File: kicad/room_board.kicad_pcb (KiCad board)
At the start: 2 copper layers, 40.6 x 58.4 mm, 21 parts, among them K1 CONN_3, U1 MSP430G2452IN20, U2 7805, U3 DHT

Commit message: update files sent to osh park for board creation
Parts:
- added HDR5: AB2_HDR02-1, ab2_header:AB2_HDR_M02-1V, F.Cu at (115.6, 54.6)
- moved SYM 10.2 mm to (114.3, 66.0)
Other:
- board text added: "2014-10-05"
- board text removed: "2014-10-01"
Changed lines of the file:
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@@
-(kicad_pcb (version 4) (host pcbnew "(2014-09-18 BZR 5141)-product")
+(kicad_pcb (version 4) (host pcbnew "(2014-10-04 BZR 5163)-product")
   (general
-    (links 46)
+    (links 48)
     (no_connects 0)
-    (area 102.679499 48.069499 143.700501 106.870501)
+    (area 89.565478 48.069499 155.318334 112.490001)
     (thickness 1.6)
     (drawings 18)
     (tracks 127)
     (zones 0)
-    (modules 21)
+    (modules 22)
     (nets 26)
   )
   (page A4)
   (layers
-    (0 F.Cu signal)
+    (0 F.Cu signal hide)
     (31 B.Cu signal)
     (32 B.Adhes user)
@@
   )
   (setup
-    (last_trace_width 0.8128)
+    (last_trace_width 0.254)
     (user_trace_width 0.254)
     (user_trace_width 0.381)
@@
     (visible_elements FFFFFF7F)
     (pcbplotparams
-      (layerselection 0x03fff_00000000)
-      (usegerberextensions false)
+      (layerselection 0x03fff_80000001)
+      (usegerberextensions true)
       (excludeedgelayer true)
       (linewidth 0.100000)
@@
   )
   (module Symbols:Symbol_OSHW-Logo_SilkScreen (layer B.Cu)
-    (at 114.3 55.88)
+    (at 114.3 66.04)
     (descr "Symbol, OSHW-Logo, Silk Screen,")
     (tags "Symbol, OSHW-Logo, Silk Screen,")
@@
     (fp_line (start 0.35052 -0.89916) (end 0.7493 -1.89992) (layer B.SilkS) (width 0.381))
   )
+  (module ab2_header:AB2_HDR_M02-1V (layer F.Cu)
+    (at 115.57 54.61 90)
+    (fp_text reference HDR5 (at 0 2.54 90) (layer F.SilkS)
+      (effects (font (size 0.8128 0.8128) (thickness 0.0762)))
+    )
+    (fp_text value AB2_HDR02-1 (at 0 -2.54 90) (layer F.SilkS)
+      (effects (font (size 0.8128 0.8128) (thickness 0.0762)))
+    )
+    (fp_line (start -1.905 -1.27) (end -0.635 -1.27) (layer F.SilkS) (width 0.127))
+    (fp_line (start -0.635 -1.27) (end 0 -0.635) (layer F.SilkS) (width 0.127))
+    (fp_line (start 0 -0.635) (end 0.635 -1.27) (layer F.SilkS) (width 0.127))
+    (fp_line (start 0.635 -1.27) (end 1.905 -1.27) (layer F.SilkS) (width 0.127))
+    (fp_line (start 1.905 -1.27) (end 2.54 -0.635) (layer F.SilkS) (width 0.127))
+    (fp_line (start 2.54 -0.635) (end 2.54 0.635) (layer F.SilkS) (width 0.127))
+    (fp_line (start 2.54 0.635) (end 1.905 1.27) (layer F.SilkS) (width 0.127))
+    (fp_line (start 1.905 1.27) (end 0.635 1.27) (layer F.SilkS) (width 0.127))
+    (fp_line (start 0.635 1.27) (end 0 0.635) (layer F.SilkS) (width 0.127))
+    (fp_line (start 0 0.635) (end -0.635 1.27) (layer F.SilkS) (width 0.127))
+    (fp_line (start -0.635 1.27) (end -1.905 1.27) (layer F.SilkS) (width 0.127))
+    (fp_line (start -1.905 1.27) (end -2.54 0.635) (layer F.SilkS) (width 0.127))
+    (fp_line (start -2.54 0.635) (end -2.54 -0.635) (layer F.SilkS) (width 0.127))
+    (fp_line (start -2.54 -0.635) (end -1.905 -1.27) (layer F.SilkS) (width 0.127))
+    (pad 1 thru_hole rect (at -1.27 0 90) (size 1.6764 1.6764) (drill 1.016) (layers *.Cu *.Mask F.SilkS)
+      (net 1 +5V))
+    (pad 2 thru_hole circle (at 1.27 0 90) (size 1.6764 1.6764) (drill 1.016) (layers *.Cu *.Mask F.SilkS)
+      (net 2 GND))
+    (model ab2_header/AB2_HDR_M01-1V.wrl
+      (at (xyz -0.05 0 0))
+      (scale (xyz 0.3937 0.3937 0.3937))
+      (rotate (xyz 0 0 0))
+    )
+    (model ab2_header/AB2_HDR_M01-1V.wrl
+      (at (xyz 0.05 0 0))
+      (scale (xyz 0.3937 0.3937 0.3937))
+      (rotate (xyz 0 0 0))
+    )
+  )
   (gr_text PROGRAM (at 138.43 81.28 90) (layer F.SilkS)
     (effects (font (size 1 1) (thickness 0.25)))
@@
     (effects (font (size 1 1) (thickness 0.25)))
   )
-  (gr_text 2014-10-01 (at 104.14 54.61 90) (layer F.SilkS)
+  (gr_text 2014-10-05 (at 104.14 54.61 90) (layer F.SilkS)
     (effects (font (size 1 1) (thickness 0.25)))
   )
-  (gr_text PIR (at 111.76 54.61 90) (layer F.SilkS)
+  (gr_text PIR (at 109.22 63.5 90) (layer F.SilkS)
     (effects (font (size 1 1) (thickness 0.25)))
   )

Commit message: update kicad schematic
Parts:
- HDR2: value AB2_HDR04-2 -> NRF24L01
- HDR4: value AB2_HDR03-1 -> PROGRAM
- HDR5: value AB2_HDR02-1 -> POWER
- U1: value MSP430G2452IN20 -> MSP430G2553IN20
- moved U1 0.13 mm to (120.8, 88.9)

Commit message: move dht to border
The former position of the DHT was under the nrf24l01.
Fixes #4.
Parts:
- added HDR6: EN_POWER_LED, ab2_header:AB2_HDR_M02-1V, F.Cu at (114.6, 64.8)
- moved U3 8.53 mm to (137.7, 91.4)
- moved SYM 7.47 mm to (106.9, 67.3)
- moved D1 2.41 mm to (139.6, 102.9)
- moved R4 1.65 mm to (121.5, 67.3)
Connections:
- R4 pad 1: +3.3V -> Net-(HDR6-Pad2)
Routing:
- net GND: track 147.7 -> 125.2 mm
- net /DHT_DATA: track 10.2 -> 17.6 mm
- net Net-(HDR6-Pad2): track 0.00 -> 3.70 mm
- net /MOSI: track 25.0 -> 28.4 mm
- net Net-(D1-Pad1): track 5.08 -> 7.49 mm
- net /MISO: track 26.2 -> 28.6 mm
- net Net-(D3-Pad1): track 4.34 -> 5.99 mm
- net +3.3V: track 97.1 -> 98.1 mm
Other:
- board text added: "room board v0.2"
- board text removed: "room board v0.1"

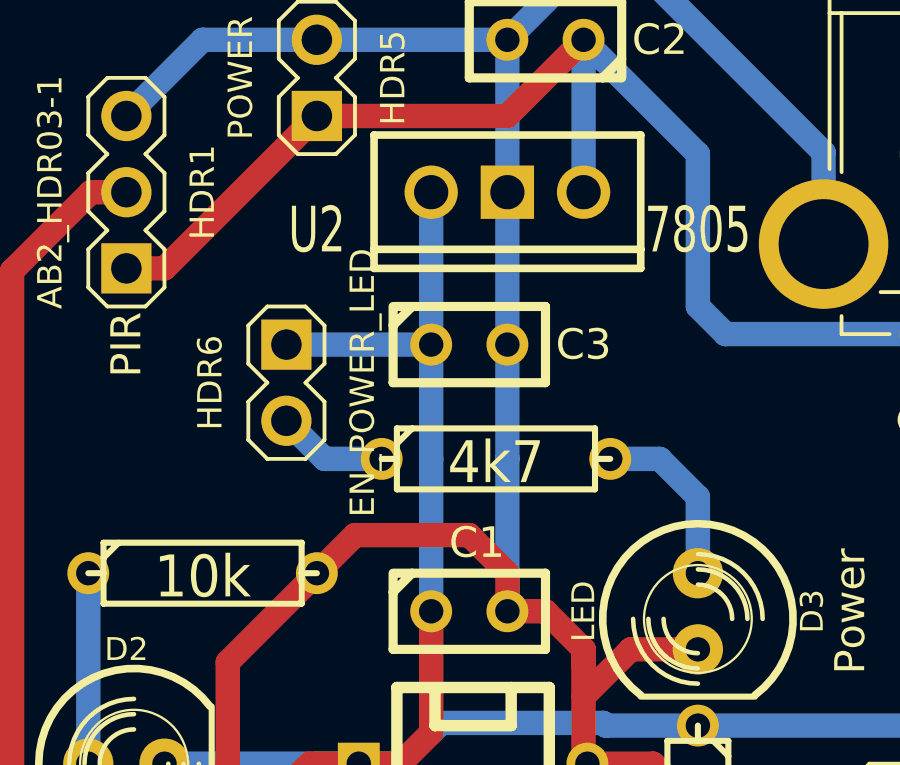
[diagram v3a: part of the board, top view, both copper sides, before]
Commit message: replace capacitory with electrolytic version
The LCV33CV needs an electrolytic capacitor on it's output.
Fix in schematic and pcb.
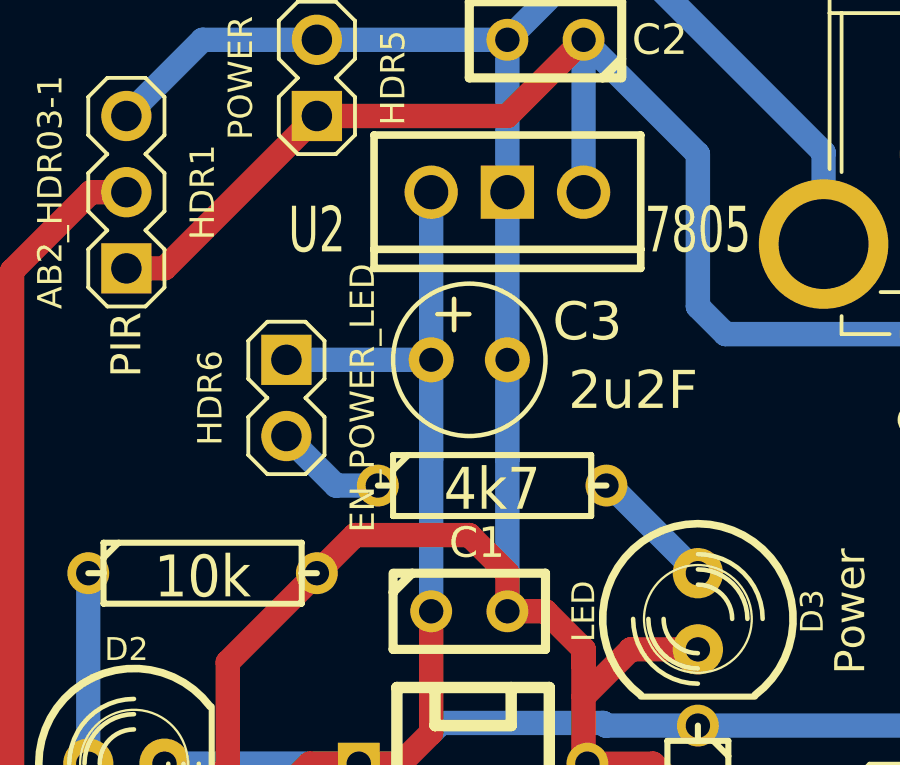
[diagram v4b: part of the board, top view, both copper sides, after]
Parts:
- removed SYM: Symbol_OSHW-Logo_SilkScreen_07Jul2012, Symbols:Symbol_OSHW-Logo_SilkScreen
- C3: footprint Discret:C1 -> Capacitors_Elko_ThroughHole:Elko_vert_11x5mm_RM2.5
- moved C3 1.37 mm to (119.4, 64.0)
- moved R4 0.90 mm to (121.4, 68.2)
- moved HDR6 0.51 mm to (114.6, 65.3)
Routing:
- net Net-(D3-Pad1): track 5.99 -> 4.26 mm

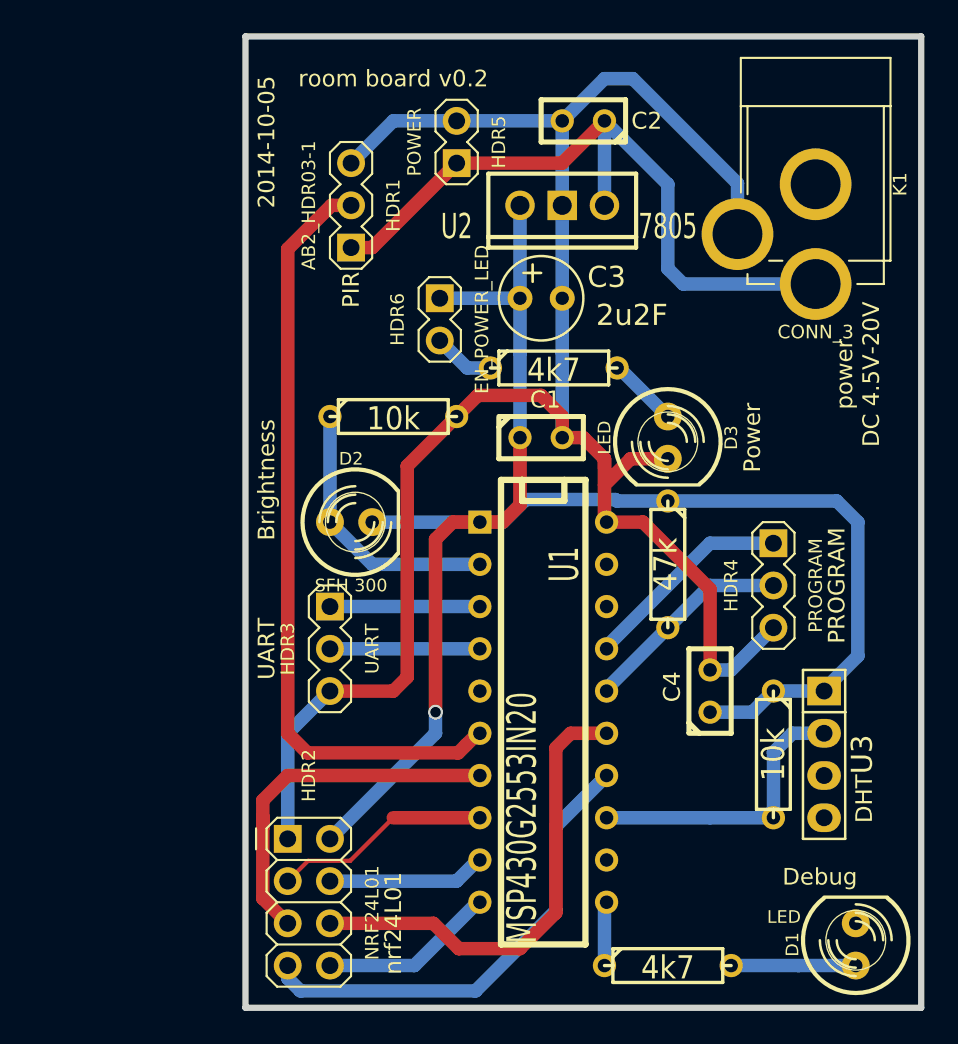
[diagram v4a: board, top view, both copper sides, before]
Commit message: update schematic/layout
- replace LM7805 symbol with LM33CV in schematic and layout
- add 3.3V power connector in schematic and layout
- replace 3pin uart with 6pin. only in schematic not done yet in layout
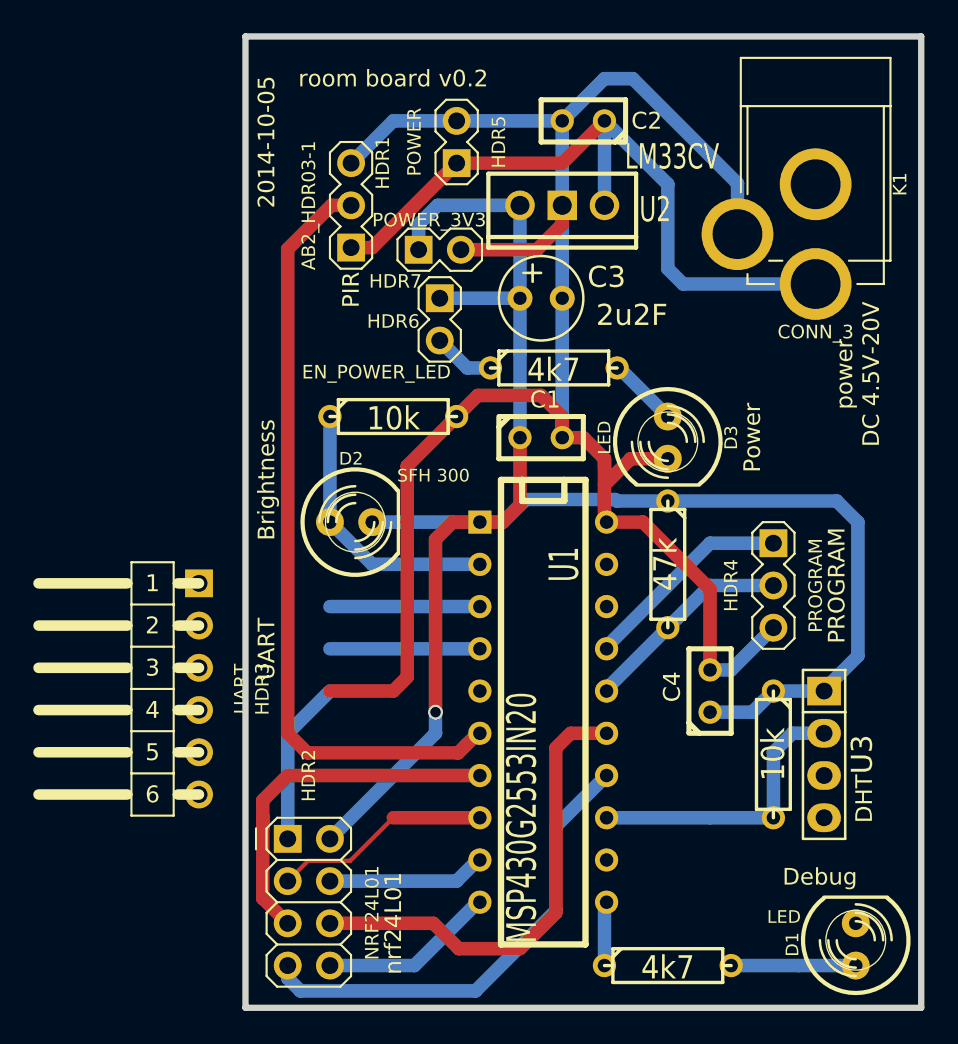
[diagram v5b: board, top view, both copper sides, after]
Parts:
- added HDR7: POWER_3V3, ab2_header:AB2_HDR_M02-1V, F.Cu at (114.6, 61.1)
- HDR3: footprint ab2_header:AB2_HDR_M03-1V -> ab2_header:AB2_HDR_M06-1H-L
- U2: value 7805 -> LM33CV
- moved HDR3 8.24 mm to (100.1, 87.5)
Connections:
- HDR3 pad 1: /RX -> GND
- HDR3 pad 2: /TX -> Net-(HDR3-Pad2)
- HDR3 pad 3: GND -> Net-(HDR3-Pad3)
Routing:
- net +3.3V: track 98.1 -> 106.2 mm
- net GND: track 125.2 -> 133.1 mm

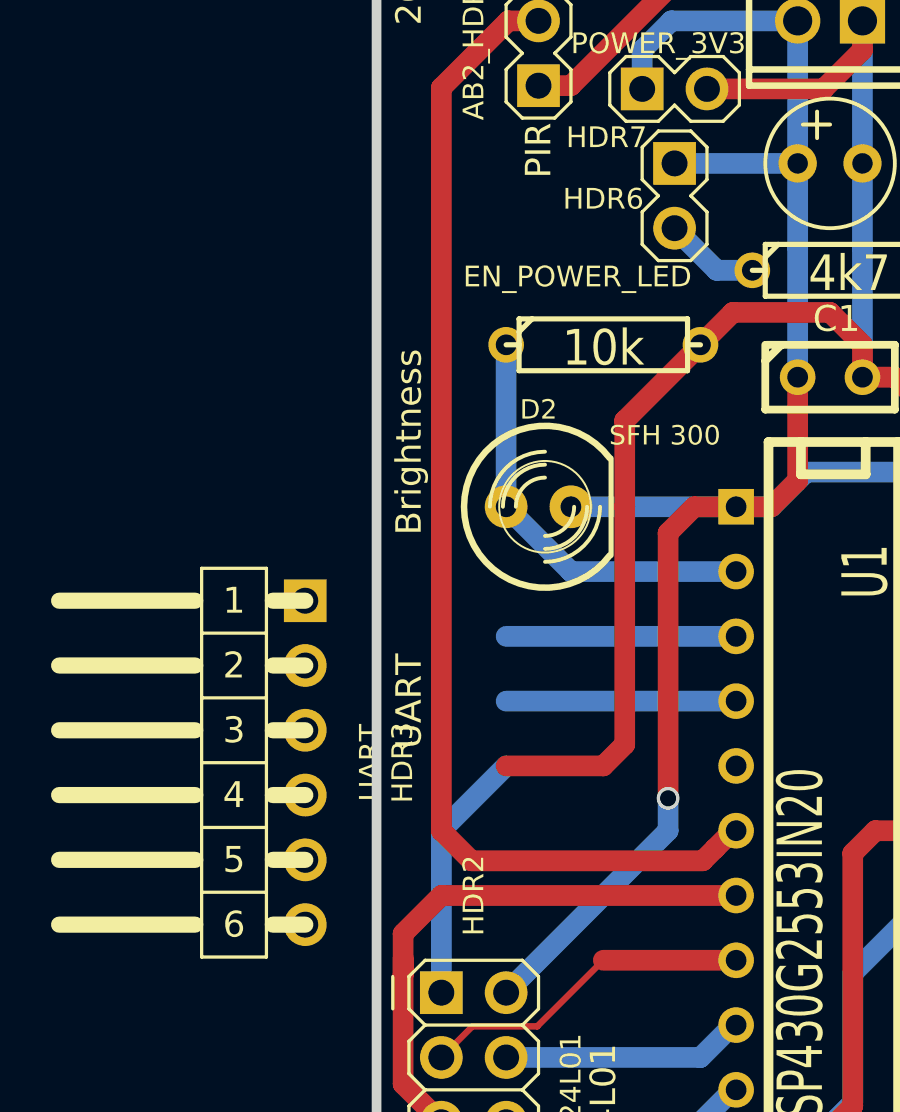
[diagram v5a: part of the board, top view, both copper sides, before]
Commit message: fix layout of uart connector
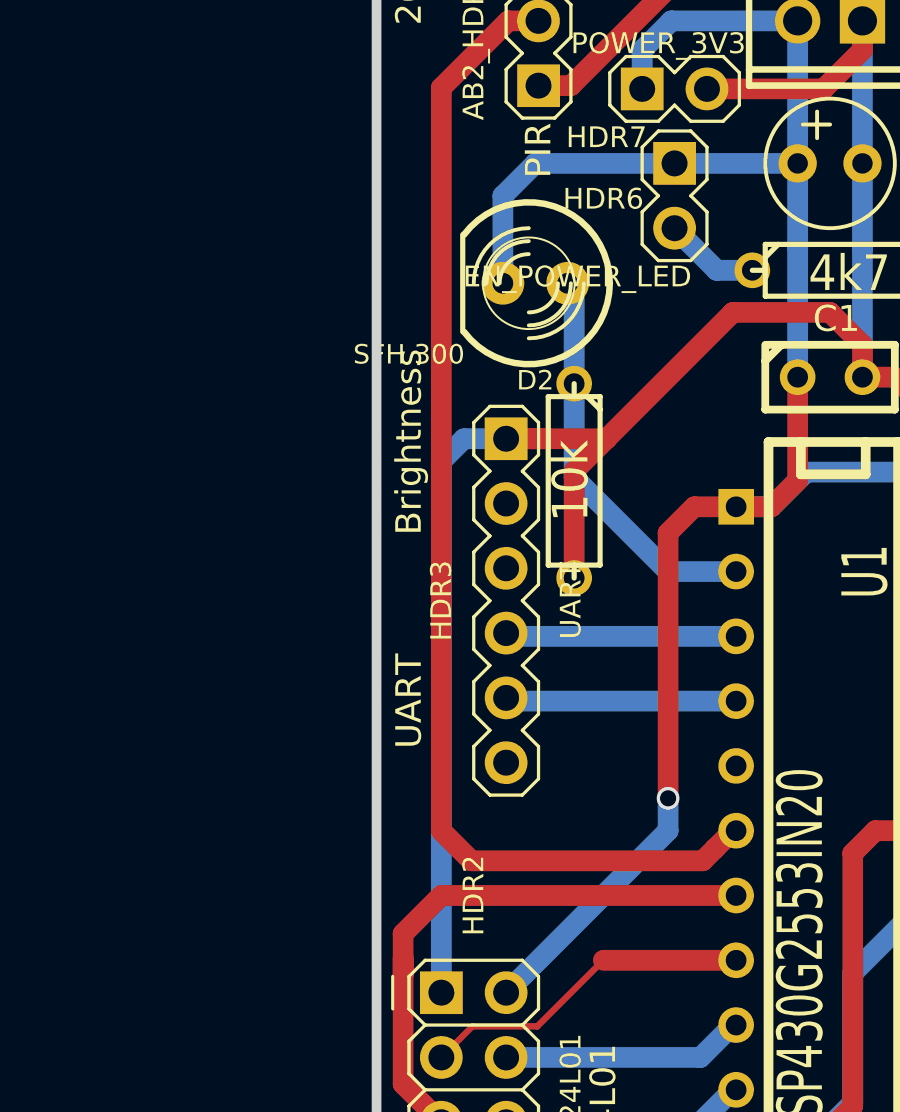
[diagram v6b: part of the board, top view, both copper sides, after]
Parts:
- HDR3: footprint ab2_header:AB2_HDR_M06-1H-L -> ab2_header:AB2_HDR_M06-1V
- moved HDR3 10.1 mm to (108.0, 81.2)
- moved D2 8.76 mm to (109.1, 68.7), turned to 180 degrees
- moved R3 5.46 mm to (110.6, 76.5), turned to 270 degrees
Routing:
- net GND: track 133.1 -> 143.1 mm
- net +3.3V: track 106.2 -> 110.5 mm
- net /BRIGHTNESS: track 16.3 -> 15.6 mm
